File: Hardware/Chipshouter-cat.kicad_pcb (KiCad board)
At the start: 2 copper layers, 36.8 x 104 mm, 76 parts, among them J1 Antenna, J2 BG306-02-A-2-0400-L-G, J3 Header7, J4 Header 2, J5 Header 4, J6 Input Power:2x AA Battery, P1 USB_C_Plug_USB2.0, Q1 AO3422, Q2 AO3422, Q3 LDA111STR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

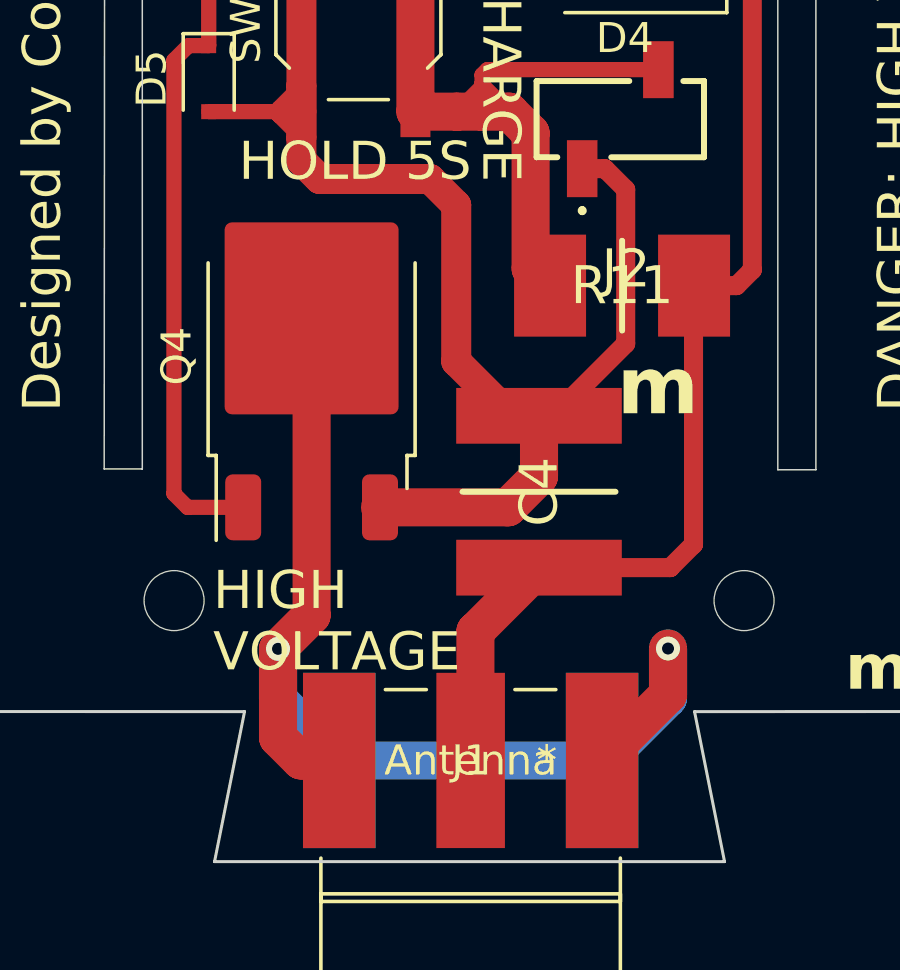
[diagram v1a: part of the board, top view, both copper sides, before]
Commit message: Changed antenna routing
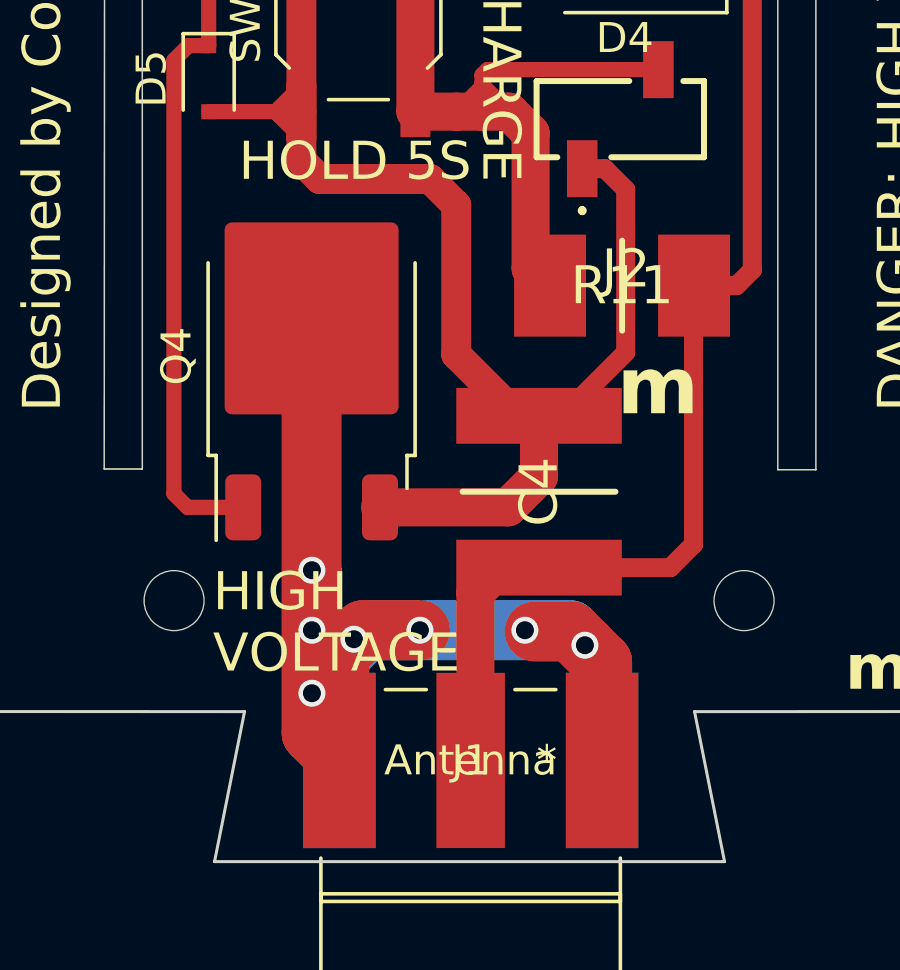
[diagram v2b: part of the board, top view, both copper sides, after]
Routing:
- net Net-(J1-Ext): track 39.5 -> 50.8 mm, vias 2 -> 7
- net Net-(D4-K): track 35.8 -> 36.5 mm
